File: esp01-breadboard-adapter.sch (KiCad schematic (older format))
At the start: 3 parts, among them P1 CONN_02X04, P2 CONN_01X04, P3 CONN_01X04

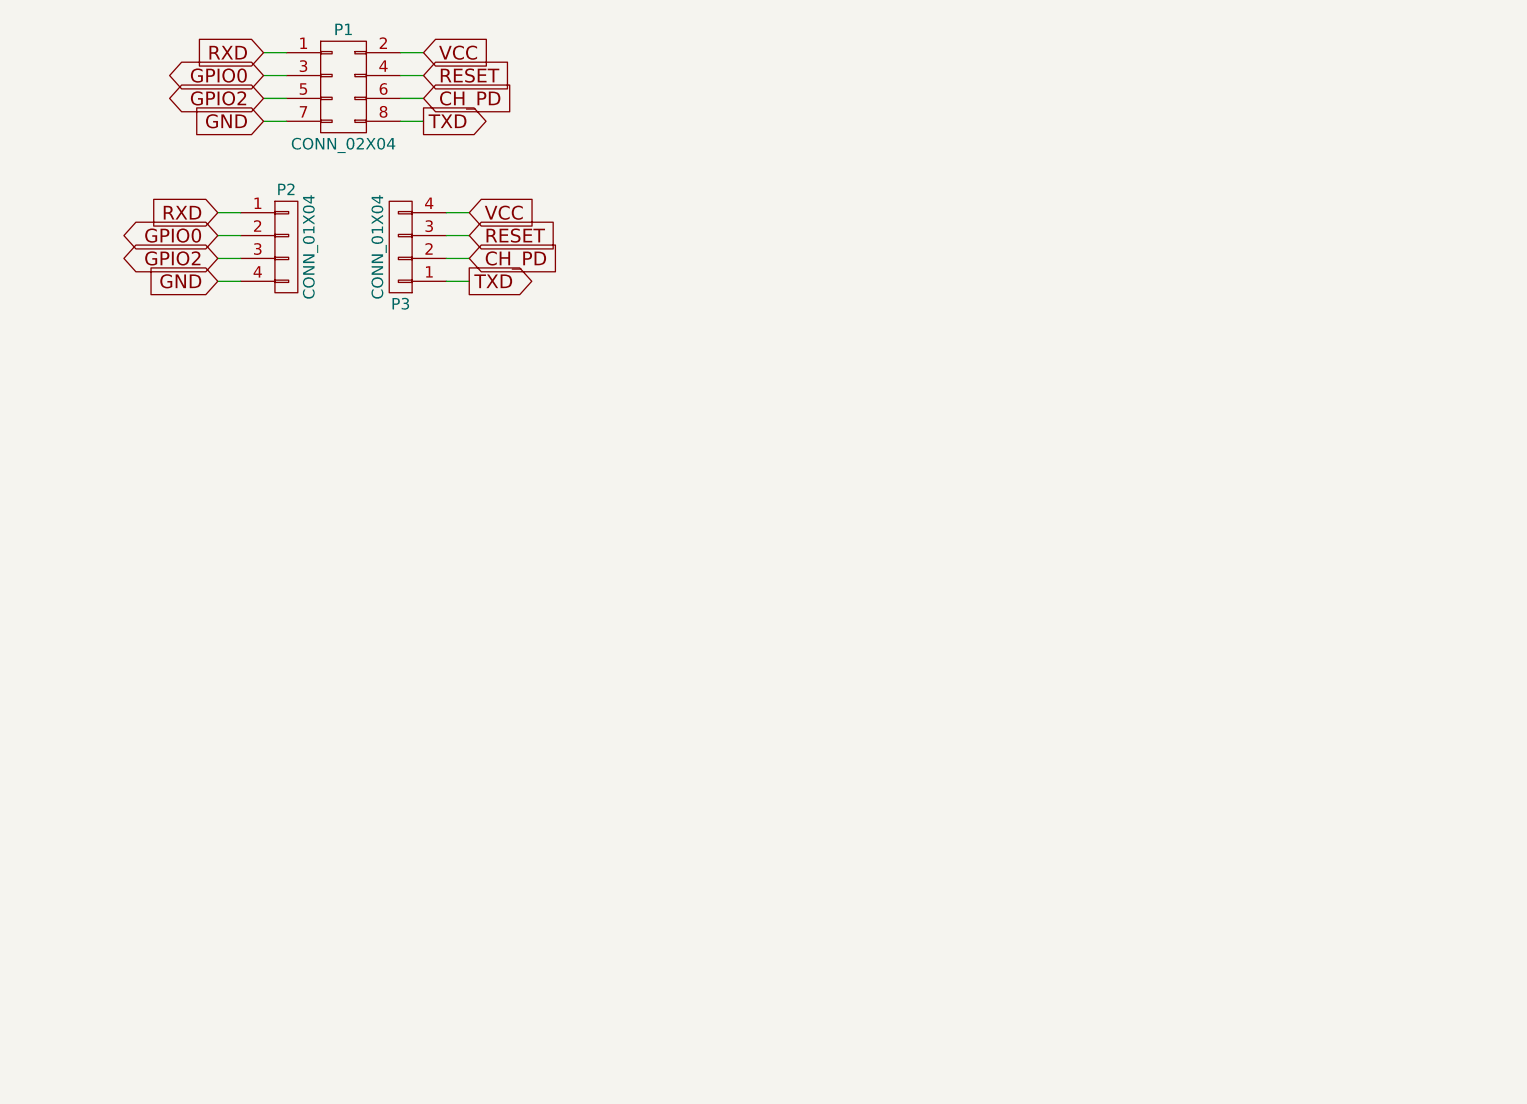
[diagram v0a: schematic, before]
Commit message: added cap to schematic
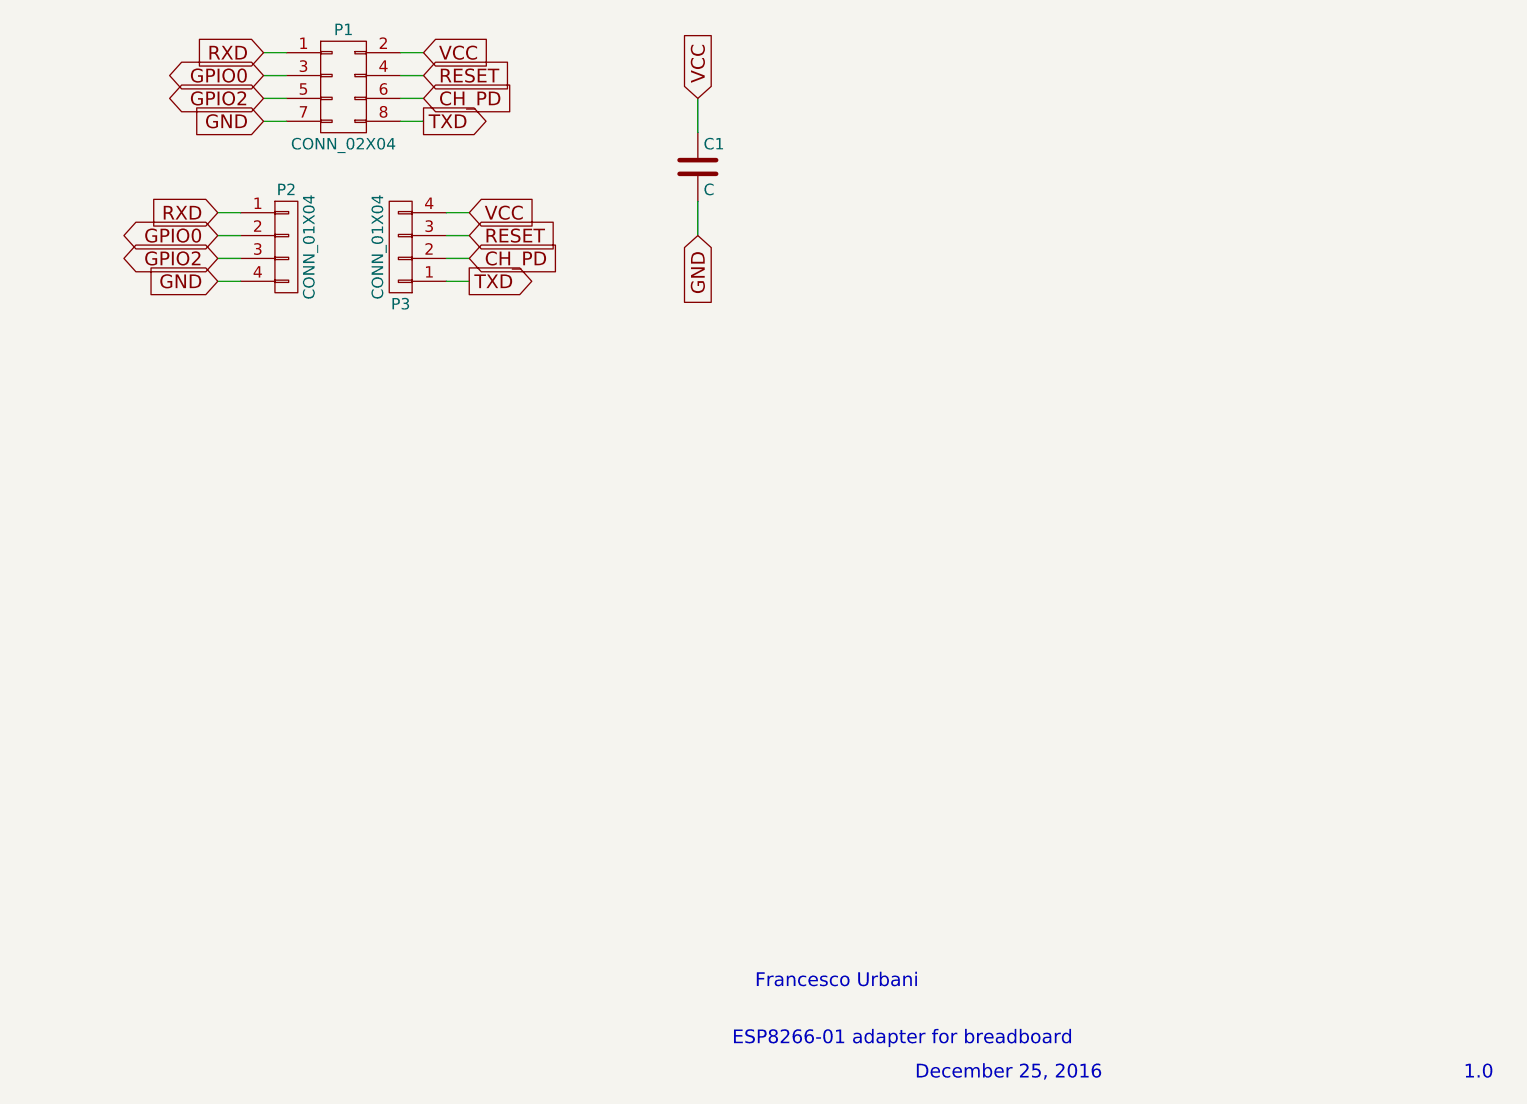
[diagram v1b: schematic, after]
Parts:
- added C1: C, Capacitors_SMD:C_1206, symbol C
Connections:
- net GND: now also C1.2
- net VCC: now also C1.1
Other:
- note added: "1.0\n"
- note added: "December 25, 2016\n"
- note added: "ESP8266-01 adapter for breadboard"
- note added: "Francesco Urbani\n"
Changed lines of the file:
@@
 Text GLabel 5100 4150 0    60   Input ~ 0
 GND
+$Comp
+L C C1
+U 1 1 585F8F92
+P 7200 3650
+F 0 "C1" H 7225 3750 50  0000 L CNN
+F 1 "C" H 7225 3550 50  0000 L CNN
+F 2 "Capacitors_SMD:C_1206" H 7238 3500 50  0001 C CNN
+F 3 "" H 7200 3650 50  0000 C CNN
+	1    7200 3650
+	1    0    0    -1
+$EndComp
+Wire Wire Line
+	7200 3500 7200 3350
+Wire Wire Line
+	7200 3800 7200 3950
+Text GLabel 7200 3350 1    60   Input ~ 0
+VCC
+Text GLabel 7200 3950 3    60   Input ~ 0
+GND
+Text Notes 7350 7500 0    60   ~ 0
+ESP8266-01 adapter for breadboard
+Text Notes 8150 7650 0    60   ~ 0
+December 25, 2016\n
+Text Notes 10550 7650 0    60   ~ 0
+1.0\n
+Text Notes 7450 7250 0    60   ~ 0
+Francesco Urbani\n
 $EndSCHEMATC

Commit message: begin 2nd layer pcb
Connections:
- net CH_PD: now also P3.3 (P3); no longer P3.2 (P2)
- net GND: now also P3.2 (P2); no longer P2.4 (P4)
- net GPIO0: now also P2.1 (P1); no longer P2.2 (P2)
- net GPIO2: now also P3.4 (P4); no longer P2.3 (P3)
- net RESET: now also P2.2 (P2); no longer P3.3 (P3)
- net RXD: now also P2.3 (P3); no longer P2.1 (P1)
- net VCC: now also P2.4 (P4); no longer P3.4 (P4)
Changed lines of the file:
@@
-GND
-$Comp
-L CONN_01X04 P3
-U 1 1 585E6908
-P 5900 4000
-F 0 "P3" H 5900 4250 50  0000 C CNN
-F 1 "CONN_01X04" V 6000 4000 50  0000 C CNN
-F 2 "Pin_Headers:Pin_Header_Straight_1x04" H 5900 4000 50  0001 C CNN
-F 3 "" H 5900 4000 50  0000 C CNN
-	1    5900 4000
-	-1   0    0    1
-$EndComp
-$Comp
-L CONN_01X04 P2
-U 1 1 585E69F1
-P 5400 4000
-F 0 "P2" H 5400 4250 50  0000 C CNN
-F 1 "CONN_01X04" V 5500 4000 50  0000 C CNN
-F 2 "Pin_Headers:Pin_Header_Straight_1x04" H 5400 4000 50  0001 C CNN
-F 3 "" H 5400 4000 50  0000 C CNN
-	1    5400 4000
-	1    0    0    -1
-$EndComp
-Wire Wire Line
-	6100 3850 6200 3850
-Wire Wire Line
-	6100 3950 6200 3950
-Wire Wire Line
-	6100 4050 6200 4050
-Wire Wire Line
-	6100 4150 6200 4150
-Text GLabel 6200 3850 2    60   Input ~ 0
-VCC
-Text GLabel 6200 3950 2    60   Input ~ 0
-RESET
-Text GLabel 6200 4050 2    60   Input ~ 0
-CH_PD
-Text GLabel 6200 4150 2    60   Output ~ 0
-TXD
-Wire Wire Line
-	5200 4150 5100 4150
-Wire Wire Line
-	5200 4050 5100 4050
-Wire Wire Line
-	5200 3950 5100 3950
-Wire Wire Line
-	5200 3850 5100 3850
-Text GLabel 5100 3850 0    60   Input ~ 0
-RXD
-Text GLabel 5100 3950 0    60   BiDi ~ 0
-GPIO0
-Text GLabel 5100 4050 0    60   BiDi ~ 0
-GPIO2
-Text GLabel 5100 4150 0    60   Input ~ 0
 GND
 $Comp
@@
 Text Notes 7450 7250 0    60   ~ 0
 Francesco Urbani\n
+$Comp
+L CONN_01X04 P3
+U 1 1 585F9D0E
+P 5950 4150
+F 0 "P3" H 5950 4400 50  0000 C CNN
+F 1 "CONN_01X04" V 6050 4150 50  0000 C CNN
+F 2 "Pin_Headers:Pin_Header_Straight_1x04" H 5950 4150 50  0001 C CNN
+F 3 "" H 5950 4150 50  0000 C CNN
+	1    5950 4150
+	-1   0    0    1
+$EndComp
+$Comp
+L CONN_01X04 P2
+U 1 1 585F9D14
+P 5450 4150
+F 0 "P2" H 5450 4400 50  0000 C CNN
+F 1 "CONN_01X04" V 5550 4150 50  0000 C CNN
+F 2 "Pin_Headers:Pin_Header_Straight_1x04" H 5450 4150 50  0001 C CNN
+F 3 "" H 5450 4150 50  0000 C CNN
+	1    5450 4150
+	1    0    0    -1
+$EndComp
+Wire Wire Line
+	6150 4000 6250 4000
+Wire Wire Line
+	6150 4100 6250 4100
+Wire Wire Line
+	6150 4200 6250 4200
+Wire Wire Line
+	6150 4300 6250 4300
+Text GLabel 6250 4000 2    60   BiDi ~ 0
+GPIO2
+Text GLabel 6250 4100 2    60   Input ~ 0
+CH_PD
+Text GLabel 6250 4200 2    60   Input ~ 0
+GND
+Text GLabel 6250 4300 2    60   Output ~ 0
+TXD
+Wire Wire Line
+	5250 4300 5150 4300
+Wire Wire Line
+	5250 4200 5150 4200
+Wire Wire Line
+	5250 4100 5150 4100
+Wire Wire Line
+	5250 4000 5150 4000
+Text GLabel 5150 4000 0    60   BiDi ~ 0
+GPIO0
+Text GLabel 5150 4100 0    60   Input ~ 0
+RESET
+Text GLabel 5150 4200 0    60   Input ~ 0
+RXD
+Text GLabel 5150 4300 0    60   Input ~ 0
+VCC
 $EndSCHEMATC

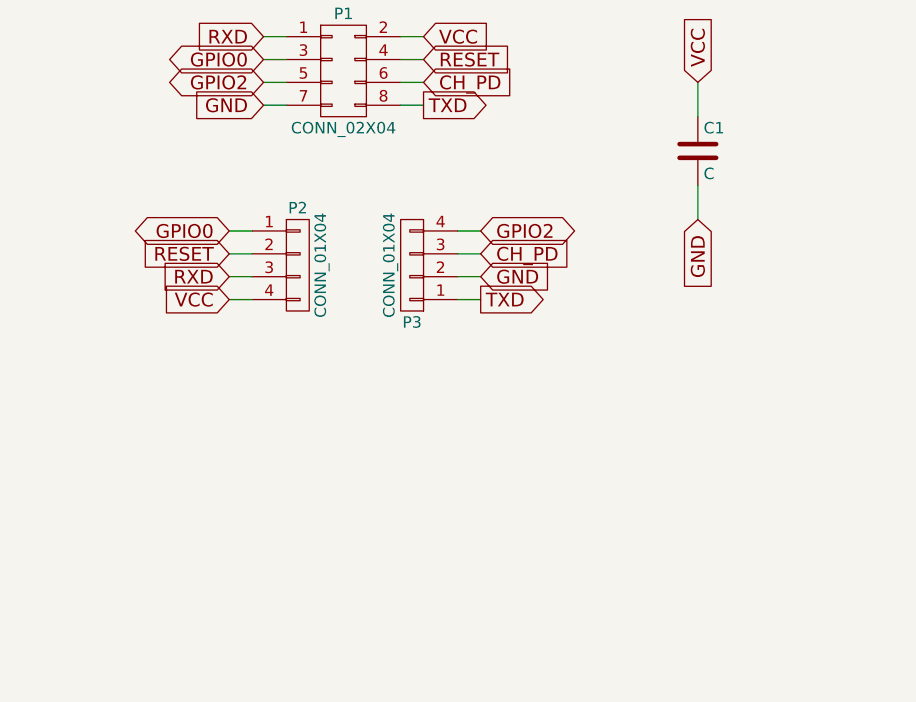
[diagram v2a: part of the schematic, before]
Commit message: added led on gpio2
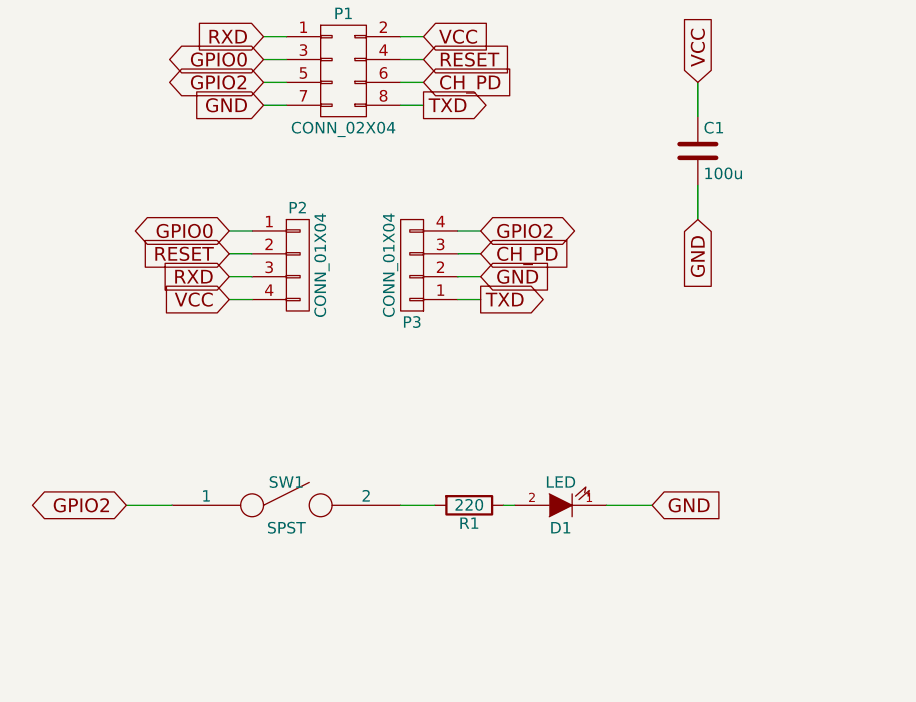
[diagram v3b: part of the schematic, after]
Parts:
- added D1: LED, LEDs:LED_0805, symbol LED
- added R1: 220, Resistors_SMD:R_0805_HandSoldering, symbol R
- added SW1: SPST, Buttons_Switches_SMD:SW_SPST_EVPBF, symbol SPST
- C1: value C -> 100u
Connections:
- net GND: now also D1.1 (K)
- net GPIO2: now also SW1.1
- new net: R1.2, SW1.2
- new net: D1.2 (A), R1.1
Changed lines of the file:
@@
 P 7200 3650
 F 0 "C1" H 7225 3750 50  0000 L CNN
-F 1 "C" H 7225 3550 50  0000 L CNN
+F 1 "100u" H 7225 3550 50  0000 L CNN
 F 2 "Capacitors_SMD:C_1206" H 7238 3500 50  0001 C CNN
 F 3 "" H 7200 3650 50  0000 C CNN
@@
 Text GLabel 5150 4300 0    60   Input ~ 0
 VCC
+$Comp
+L SPST SW1
+U 1 1 586223A9
+P 5400 5200
+F 0 "SW1" H 5400 5300 50  0000 C CNN
+F 1 "SPST" H 5400 5100 50  0000 C CNN
+F 2 "Buttons_Switches_SMD:SW_SPST_EVPBF" H 5400 5200 50  0001 C CNN
+F 3 "" H 5400 5200 50  0000 C CNN
+	1    5400 5200
+	1    0    0    -1
+$EndComp
+$Comp
+L R R1
+U 1 1 586223E4
+P 6200 5200
+F 0 "R1" V 6280 5200 50  0000 C CNN
+F 1 "220" V 6200 5200 50  0000 C CNN
+F 2 "Resistors_SMD:R_0805_HandSoldering" V 6130 5200 50  0001 C CNN
+F 3 "" H 6200 5200 50  0000 C CNN
+	1    6200 5200
+	0    1    1    0
+$EndComp
+$Comp
+L LED D1
+U 1 1 58622421
+P 6600 5200
+F 0 "D1" H 6600 5300 50  0000 C CNN
+F 1 "LED" H 6600 5100 50  0000 C CNN
+F 2 "LEDs:LED_0805" H 6600 5200 50  0001 C CNN
+F 3 "" H 6600 5200 50  0000 C CNN
+	1    6600 5200
+	-1   0    0    1
+$EndComp
+Text GLabel 7000 5200 2    60   Input ~ 0
+GND
+Text GLabel 4700 5200 0    60   BiDi ~ 0
+GPIO2
+Wire Wire Line
+	4700 5200 4900 5200
+Wire Wire Line
+	5900 5200 6050 5200
+Wire Wire Line
+	6350 5200 6400 5200
+Wire Wire Line
+	6800 5200 7000 5200
 $EndSCHEMATC

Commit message: pcb complete
pcb complete with signed bottom sikscreen
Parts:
- removed D1: LED, LEDs:LED_0805, symbol LED
- removed R1: 220, Resistors_SMD:R_0805_HandSoldering, symbol R
- removed SW1: SPST, Buttons_Switches_SMD:SW_SPST_EVPBF, symbol SPST
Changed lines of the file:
@@
 Text GLabel 5150 4300 0    60   Input ~ 0
 VCC
-$Comp
-L SPST SW1
-U 1 1 586223A9
-P 5400 5200
-F 0 "SW1" H 5400 5300 50  0000 C CNN
-F 1 "SPST" H 5400 5100 50  0000 C CNN
-F 2 "Buttons_Switches_SMD:SW_SPST_EVPBF" H 5400 5200 50  0001 C CNN
-F 3 "" H 5400 5200 50  0000 C CNN
-	1    5400 5200
-	1    0    0    -1
-$EndComp
-$Comp
-L R R1
-U 1 1 586223E4
-P 6200 5200
-F 0 "R1" V 6280 5200 50  0000 C CNN
-F 1 "220" V 6200 5200 50  0000 C CNN
-F 2 "Resistors_SMD:R_0805_HandSoldering" V 6130 5200 50  0001 C CNN
-F 3 "" H 6200 5200 50  0000 C CNN
-	1    6200 5200
-	0    1    1    0
-$EndComp
-$Comp
-L LED D1
-U 1 1 58622421
-P 6600 5200
-F 0 "D1" H 6600 5300 50  0000 C CNN
-F 1 "LED" H 6600 5100 50  0000 C CNN
-F 2 "LEDs:LED_0805" H 6600 5200 50  0001 C CNN
-F 3 "" H 6600 5200 50  0000 C CNN
-	1    6600 5200
-	-1   0    0    1
-$EndComp
-Text GLabel 7000 5200 2    60   Input ~ 0
-GND
-Text GLabel 4700 5200 0    60   BiDi ~ 0
-GPIO2
-Wire Wire Line
-	4700 5200 4900 5200
-Wire Wire Line
-	5900 5200 6050 5200
-Wire Wire Line
-	6350 5200 6400 5200
-Wire Wire Line
-	6800 5200 7000 5200
 $EndSCHEMATC

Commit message: edited schematic
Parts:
- removed P2, P3: CONN_01X04, Pin_Headers:Pin_Header_Straight_1x04, symbol CONN_01X04
- added P2: CONN_01X10, Pin_Headers:Pin_Header_Straight_1x10, symbol CONN_01X10
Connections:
- net CH_PD: now also P2.7 (P7)
- net GND: now also P2.6 (P6)
- net GPIO0: now also P2.9 (P9)
- net GPIO2: now also P2.10 (P10)
- net RESET: now also P2.8 (P8)
- net RXD: now also P2.3 (P3)
- net TXD: now also P2.2 (P2)
- net VCC: now also P2.4 (P4)
- no-connect marks 0 -> 2
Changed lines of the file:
@@
 Francesco Urbani\n
 $Comp
-L CONN_01X04 P3
-U 1 1 585F9D0E
-P 5950 4150
-F 0 "P3" H 5950 4400 50  0000 C CNN
-F 1 "CONN_01X04" V 6050 4150 50  0000 C CNN
-F 2 "Pin_Headers:Pin_Header_Straight_1x04" H 5950 4150 50  0001 C CNN
-F 3 "" H 5950 4150 50  0000 C CNN
-	1    5950 4150
-	-1   0    0    1
+L CONN_01X10 P2
+U 1 1 5862AFF5
+P 5700 4150
+F 0 "P2" H 5700 4700 50  0000 C CNN
+F 1 "CONN_01X10" V 5800 4150 50  0000 C CNN
+F 2 "Pin_Headers:Pin_Header_Straight_1x10" H 5700 4150 50  0001 C CNN
+F 3 "" H 5700 4150 50  0000 C CNN
+	1    5700 4150
+	0    -1   -1   0
 $EndComp
-$Comp
-L CONN_01X04 P2
-U 1 1 585F9D14
-P 5450 4150
-F 0 "P2" H 5450 4400 50  0000 C CNN
-F 1 "CONN_01X04" V 5550 4150 50  0000 C CNN
-F 2 "Pin_Headers:Pin_Header_Straight_1x04" H 5450 4150 50  0001 C CNN
-F 3 "" H 5450 4150 50  0000 C CNN
-	1    5450 4150
-	1    0    0    -1
-$EndComp
+Text GLabel 5350 4550 3    60   Output ~ 0
+TXD
+Text GLabel 5450 4550 3    60   Input ~ 0
+RXD
+Text GLabel 5550 4550 3    60   Input ~ 0
+VCC
+Text GLabel 5750 4550 3    60   Input ~ 0
+GND
+Text GLabel 5850 4550 3    60   Input ~ 0
+CH_PD
+Text GLabel 5950 4550 3    60   Input ~ 0
+RESET
+Text GLabel 6050 4550 3    60   BiDi ~ 0
+GPIO0
+Text GLabel 6150 4550 3    60   BiDi ~ 0
+GPIO2
 Wire Wire Line
-	6150 4000 6250 4000
+	5350 4350 5350 4550
 Wire Wire Line
-	6150 4100 6250 4100
+	5450 4550 5450 4350
 Wire Wire Line
-	6150 4200 6250 4200
+	5550 4350 5550 4550
 Wire Wire Line
-	6150 4300 6250 4300
-Text GLabel 6250 4000 2    60   BiDi ~ 0
-GPIO2
-Text GLabel 6250 4100 2    60   Input ~ 0
-CH_PD
-Text GLabel 6250 4200 2    60   Input ~ 0
-GND
-Text GLabel 6250 4300 2    60   Output ~ 0
-TXD
+	5750 4550 5750 4350
 Wire Wire Line
-	5250 4300 5150 4300
+	5850 4350 5850 4550
 Wire Wire Line
-	5250 4200 5150 4200
+	5950 4550 5950 4350
 Wire Wire Line
-	5250 4100 5150 4100
+	6050 4350 6050 4550
 Wire Wire Line
-	5250 4000 5150 4000
-Text GLabel 5150 4000 0    60   BiDi ~ 0
-GPIO0
-Text GLabel 5150 4100 0    60   Input ~ 0
-RESET
-Text GLabel 5150 4200 0    60   Input ~ 0
-RXD
-Text GLabel 5150 4300 0    60   Input ~ 0
-VCC
+	6150 4550 6150 4350
+Wire Wire Line
+	5650 4350 5650 4550
+Wire Wire Line
+	5250 4550 5250 4350
+NoConn ~ 5650 4550
+NoConn ~ 5250 4550
 $EndSCHEMATC

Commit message: new pcb layout, fix connection
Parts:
- P2: footprint Pin_Headers:Pin_Header_Straight_1x10 -> Pin_Headers:Pin_Header_Straight_1x10_Pitch2.54mm
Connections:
- net CH_PD: now also P2.8 (P8); no longer P2.7 (P7)
- net RESET: now also P2.7 (P7); no longer P2.8 (P8)
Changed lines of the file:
@@
 F 0 "P2" H 5700 4700 50  0000 C CNN
 F 1 "CONN_01X10" V 5800 4150 50  0000 C CNN
-F 2 "Pin_Headers:Pin_Header_Straight_1x10" H 5700 4150 50  0001 C CNN
+F 2 "Pin_Headers:Pin_Header_Straight_1x10_Pitch2.54mm" H 5700 4150 50  0001 C CNN
 F 3 "" H 5700 4150 50  0000 C CNN
 	1    5700 4150
@@
 Text GLabel 5750 4550 3    60   Input ~ 0
 GND
+Text GLabel 5950 4550 3    60   Input ~ 0
+CH_PD
 Text GLabel 5850 4550 3    60   Input ~ 0
-CH_PD
-Text GLabel 5950 4550 3    60   Input ~ 0
 RESET
 Text GLabel 6050 4550 3    60   BiDi ~ 0

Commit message: pcb complete
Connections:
- net CH_PD: now also P2.10 (P10); no longer P2.8 (P8)
- net GPIO0: now also P2.8 (P8); no longer P2.9 (P9)
- net GPIO2: now also P2.9 (P9); no longer P2.10 (P10)
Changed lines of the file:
@@
 Text GLabel 5750 4550 3    60   Input ~ 0
 GND
-Text GLabel 5950 4550 3    60   Input ~ 0
+Text GLabel 6150 4550 3    60   Input ~ 0
 CH_PD
 Text GLabel 5850 4550 3    60   Input ~ 0
 RESET
+Text GLabel 5950 4550 3    60   BiDi ~ 0
+GPIO0
 Text GLabel 6050 4550 3    60   BiDi ~ 0
-GPIO0
-Text GLabel 6150 4550 3    60   BiDi ~ 0
 GPIO2
 Wire Wire Line
